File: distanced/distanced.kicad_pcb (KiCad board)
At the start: 2 copper layers, 25 parts, among them Y1 Crystal

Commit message: better schematic
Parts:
- added C11: 10uF, Capacitors_SMD:C_0402, F.Cu at (155.4, 114.0)
- added C12: 10uF, Capacitors_SMD:C_0402, F.Cu at (196.3, 130.7)
- added D1: LED, LEDs:LED_0402, F.Cu at (179.4, 145.6)
- added D2: LED_GREEN, LEDs:LED_0402, F.Cu at (128.8, 114.6)
- added D3: D_Small, Diodes_SMD:D_0603, F.Cu at (160.1, 134.7)
- added E1: Econn, Pin_Headers:Pin_Header_Angled_2x02_Pitch2.54mm, F.Cu at (200.9, 70.3)
- added J1: FTDI prog, Pin_Headers:Pin_Header_Angled_1x06_Pitch2.54mm, F.Cu at (169.0, 67.7)
- added J2: ICSP, Pin_Headers:Pin_Header_Straight_2x03_Pitch2.54mm, F.Cu at (194.6, 99.6)
- added N1: Nconn, Pin_Headers:Pin_Header_Angled_2x02_Pitch2.54mm, F.Cu at (201.1, 82.1)
- added Q1: BSS138, TO_SOT_Packages_SMD:SOT-23, F.Cu at (176.7, 118.5)
- added Q2: BSS138, TO_SOT_Packages_SMD:SOT-23, F.Cu at (175.1, 106.3)
- added R10: 10K, Resistors_SMD:R_0402, F.Cu at (132.6, 78.0)
- added R11: 10K, Resistors_SMD:R_0402, F.Cu at (115.8, 50.8)
- added R8: 10K, Resistors_SMD:R_0402, F.Cu at (142.5, 64.5)
- added R9: 10K, Resistors_SMD:R_0402, F.Cu at (108.2, 140.6)
- added S1: Sconn, Pin_Headers:Pin_Header_Angled_2x02_Pitch2.54mm, F.Cu at (201.5, 60.4)
- added U1: MIC5205-2.8, TO_SOT_Packages_SMD:SOT-23-5, F.Cu at (163.5, 119.7)
- added W1: Wconn, Pin_Headers:Pin_Header_Angled_2x02_Pitch2.54mm, F.Cu at (201.5, 52.0)
- C1, C3: value (none) -> 10uF
- C4: value (none) -> 0.1uF
- R1: value (none) -> 10K
- R4: value (none) -> 330
- SWRST1: footprint Buttons_Switches_THT:SW_PUSH_6mm_h4.3mm -> Buttons_Switches_SMD:SW_SPST_B3S-1000
- Y1: value Crystal -> Crystal_GND24; footprint Crystals:Crystal_SMD_2016-4pin_2.0x1.6mm -> Crystals:Crystal_SMD_3225-4pin_3.2x2.5mm_HandSoldering
- moved LSR1 103.6 mm to (166.7, 32.5)
- moved C8 67.0 mm to (79.3, 92.6)
- moved C7 59.7 mm to (78.9, 95.9)
- moved SWRST1 25.0 mm to (84.4, 81.8)
- moved Y1 3.05 mm to (86.6, 95.5), turned to 51 degrees
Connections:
- C10 pad 1: VCC -> +2V8
- C3 pad 1: VCC -> +3V3
- C4 pad 1: VCC -> +3V3
- C5 pad 1: VCC -> +3V3
- C9 pad 1: VCC -> +2V8
- LSR1 pad 1: VCC -> +2V8
- LSR1 pad 10: A5 -> 2.8_SCL
- LSR1 pad 11: VCC -> +2V8
- LSR1 pad 5: D3 -> Net-(D3-Pad2)
- LSR1 pad 9: A4 -> 2.8_SDA
- R2 pad 1: VCC -> +3V3
- R3 pad 1: VCC -> +3V3
- R5 pad 1: VCC -> +3V3
- R6 pad 1: VCC -> +2V8
- R7 pad 1: VCC -> +2V8
- R7 pad 2: D3 -> Net-(D3-Pad2)
- RS485 pad 8: VCC -> +3V3
- Vreg1 pad 5: VCC -> +3V3
- Y1 pad 2: Net-(C8-Pad1) -> GNDREF
- Y1 pad 3: (no net) -> Net-(C8-Pad1)
- Y1 pad 4: (no net) -> GNDREF
- uC1 pad 18: VCC -> +3V3
- uC1 pad 4: VCC -> +3V3
- uC1 pad 6: VCC -> +3V3

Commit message: first routing done, ready for revision and being lectured
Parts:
- removed C10: 4.7uF, Capacitors_SMD:C_0402
- removed C9: 100nF, Capacitors_SMD:C_0402
- removed D13, PWR: , LEDs:LED_0402
- removed D3: D_Small, Diodes_SMD:D_0603
- removed LSR1: VL53L0X, VL53L0X:VL53L0X
- removed N1: Nconn, Pin_Headers:Pin_Header_Angled_2x02_Pitch2.54mm
- removed R6, R7: 10K, Resistors_SMD:R_0402
- removed S1: Sconn, Pin_Headers:Pin_Header_Angled_2x02_Pitch2.54mm
- added C13: 100nF, Capacitors_SMD:C_0402, F.Cu at (148.1, 85.6)
- added C14: 4.7uF, Capacitors_SMD:C_0402, F.Cu at (148.1, 84.5)
- added D4: D_Small, Diodes_SMD:D_0603, F.Cu at (153.0, 80.7)
- added LSR2: VL53L0X, VL53L0X:VL53L0X, F.Cu at (148.1, 88.9)
- added R12: 10K, Resistors_SMD:R_0402, F.Cu at (147.2, 92.3)
- added R13: 10K, Resistors_SMD:R_0402, F.Cu at (149.0, 92.3)
- added REF**: MountingHole_3.2mm_M3_Pad, Mounting_Holes:MountingHole_3.2mm_M3_Pad, F.Cu at (148.0, 99.0)
- added REF**: MountingHole_3.2mm_M3_Pad, Mounting_Holes:MountingHole_3.2mm_M3_Pad, F.Cu at (148.0, 70.0)
- C1, C11, C12, C3, C4, C7, C8, E1, J1, Q1, Q2, R10, R11, R2, R3, R8, R9, RS485, U1, Vreg1, W1, Y1, uC1: moved to B.Cu
- J2: footprint Pin_Headers:Pin_Header_Straight_2x03_Pitch2.54mm -> Pin_Headers:Pin_Header_Angled_2x03_Pitch2.54mm; moved to B.Cu
- moved R9 69.3 mm to (157.5, 91.8), turned to 180 degrees
- moved C7 68.6 mm to (144.1, 74.5)
- moved W1 67.1 mm to (138.5, 75.0), turned to 180 degrees
- moved C8 66.0 mm to (144.2, 80.4), turned to 180 degrees
- moved E1 65.8 mm to (138.5, 91.0), turned to 180 degrees
- moved C12 64.7 mm to (146.9, 88.9), turned to 90 degrees
- moved SWRST1 63.5 mm to (147.9, 78.7), turned to 90 degrees
- moved D1 63.4 mm to (152.0, 88.4), turned to 270 degrees
- moved Y1 60.4 mm to (144.3, 77.5), turned to 0 degrees
- moved J2 59.0 mm to (138.5, 81.5), turned to 180 degrees
- moved uC1 58.7 mm to (153.8, 79.1)
- moved C6 56.2 mm to (143.0, 74.7), turned to 180 degrees
- moved R11 54.5 mm to (156.9, 86.6), turned to 270 degrees
- moved C5 49.2 mm to (152.8, 78.1), turned to 90 degrees
- moved RS485 47.6 mm to (144.2, 84.0), turned to 0 degrees
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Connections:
- C11 pad 1: Net-(C11-Pad1) -> +3V3
- C3 pad 2: Net-(C3-Pad2) -> GNDREF
- C4 pad 2: Net-(C3-Pad2) -> GNDREF
- R1 pad 2: Net-(C3-Pad2) -> GNDREF
- Vreg1 pad 3: Net-(Vreg1-Pad3) -> RAW
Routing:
- net GNDREF: track 0.00 -> 151.1 mm, vias 0 -> 8
- net +3V3: track 0.00 -> 116.5 mm, vias 0 -> 9
- net RAW: track 0.00 -> 93.3 mm
- net DRT: track 0.00 -> 82.7 mm
- net D13: track 0.00 -> 53.6 mm, vias 0 -> 1
- net D11: track 0.00 -> 46.2 mm, vias 0 -> 2
- net B: track 0.00 -> 39.2 mm, vias 0 -> 4
- net A: track 0.00 -> 32.8 mm, vias 0 -> 1
- net D4: track 0.00 -> 31.1 mm, vias 0 -> 5
- net RXI: track 0.00 -> 31.1 mm, vias 0 -> 2
- net +2V8: track 0.00 -> 30.0 mm, vias 0 -> 4
- net D12: track 0.00 -> 26.3 mm
- net TXO: track 0.00 -> 26.3 mm, vias 0 -> 3
- net A4: track 0.00 -> 21.2 mm
- net Net-(D4-Pad2): track 0.00 -> 20.8 mm, vias 0 -> 6
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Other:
- board outline added: 29 x 41 mm
- net class Default: clearance 0.2 -> 0.00889
- rule trace_clearance: 0.2 -> 0.00889
- rule trace_min: 0.2 -> 0.0889

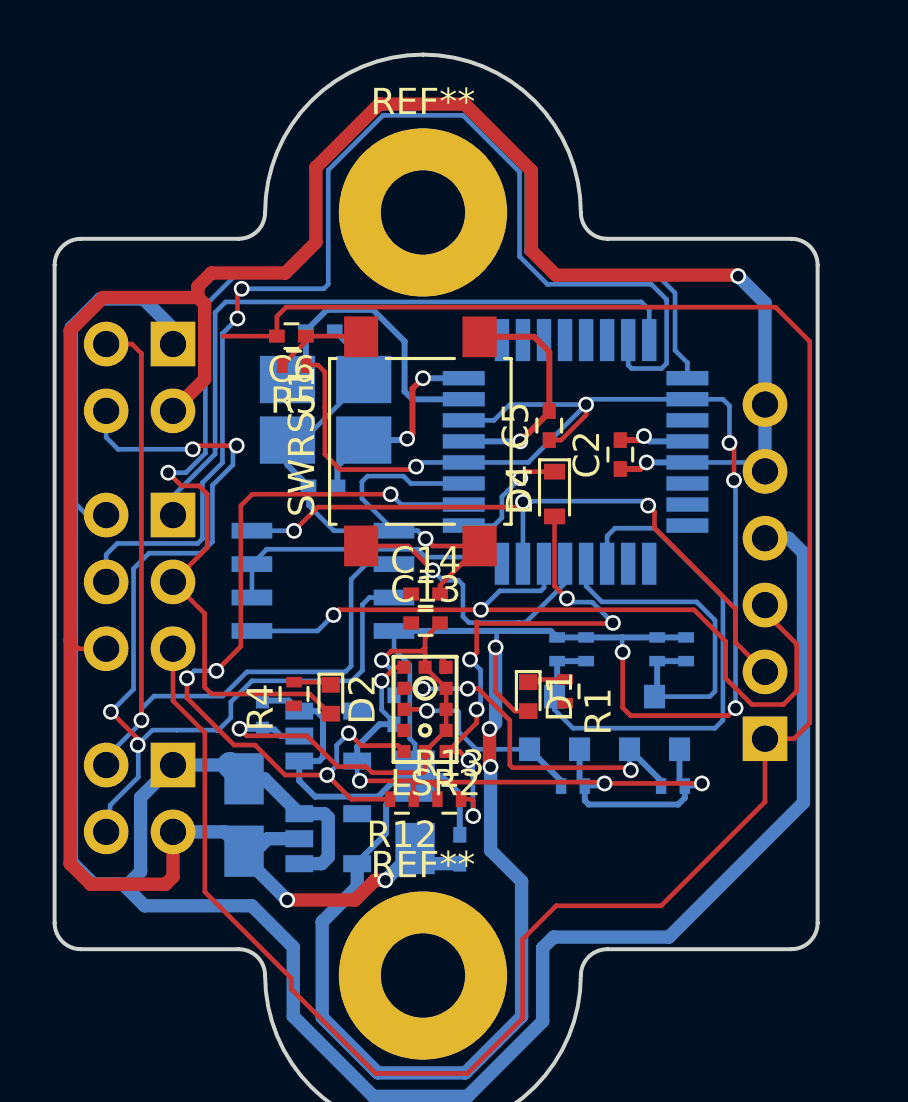
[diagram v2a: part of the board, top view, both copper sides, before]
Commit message: modified reference text on the board
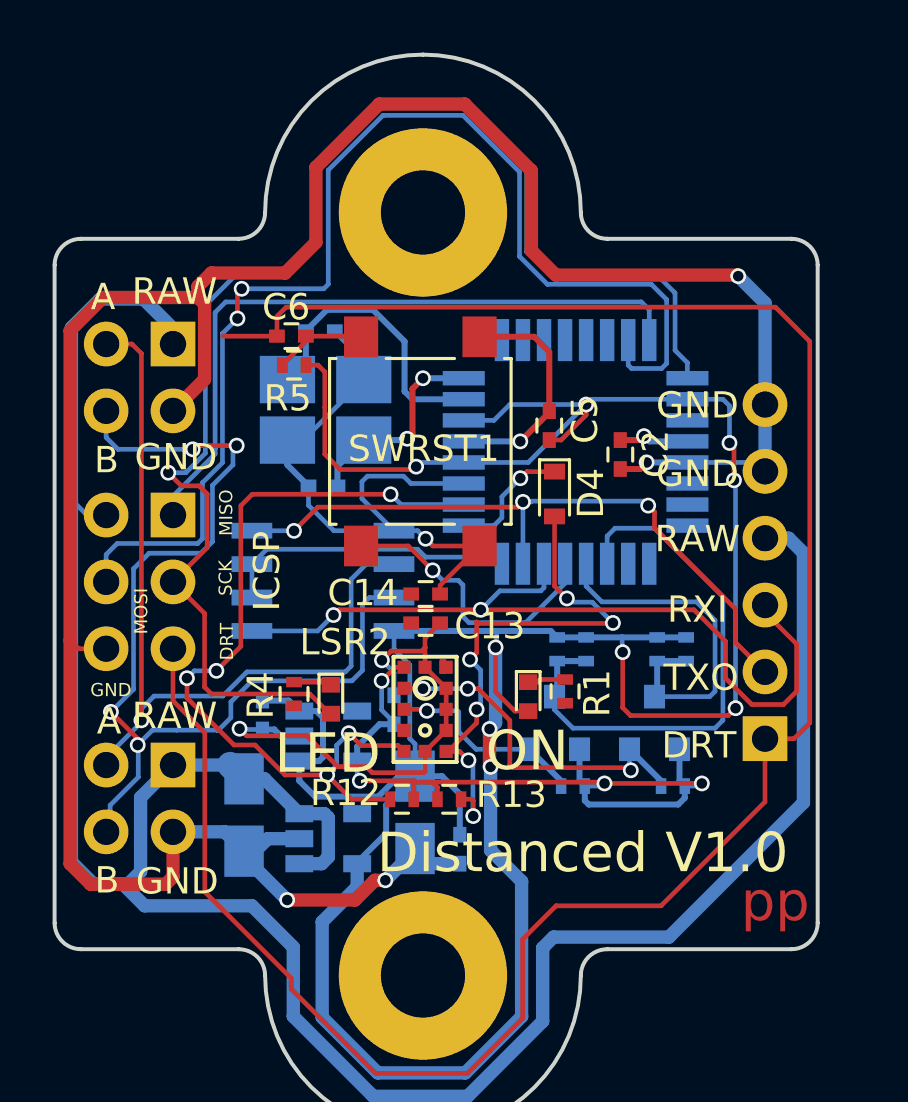
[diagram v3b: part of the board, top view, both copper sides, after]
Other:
- board text added: "A"
- board text added: "B"
- board text added: "DRT"
- board text added: "Distanced V1.0"
- board text added: "GND"
- board text added: "ICSP"
- board text added: "LED"
- board text added: "MISO"
- board text added: "MOSI"
- board text added: "ON"
- board text added: "RAW"
- board text added: "RXI"
- board text added: "SCK"
- board text added: "TXO"
- board text added: "pp"

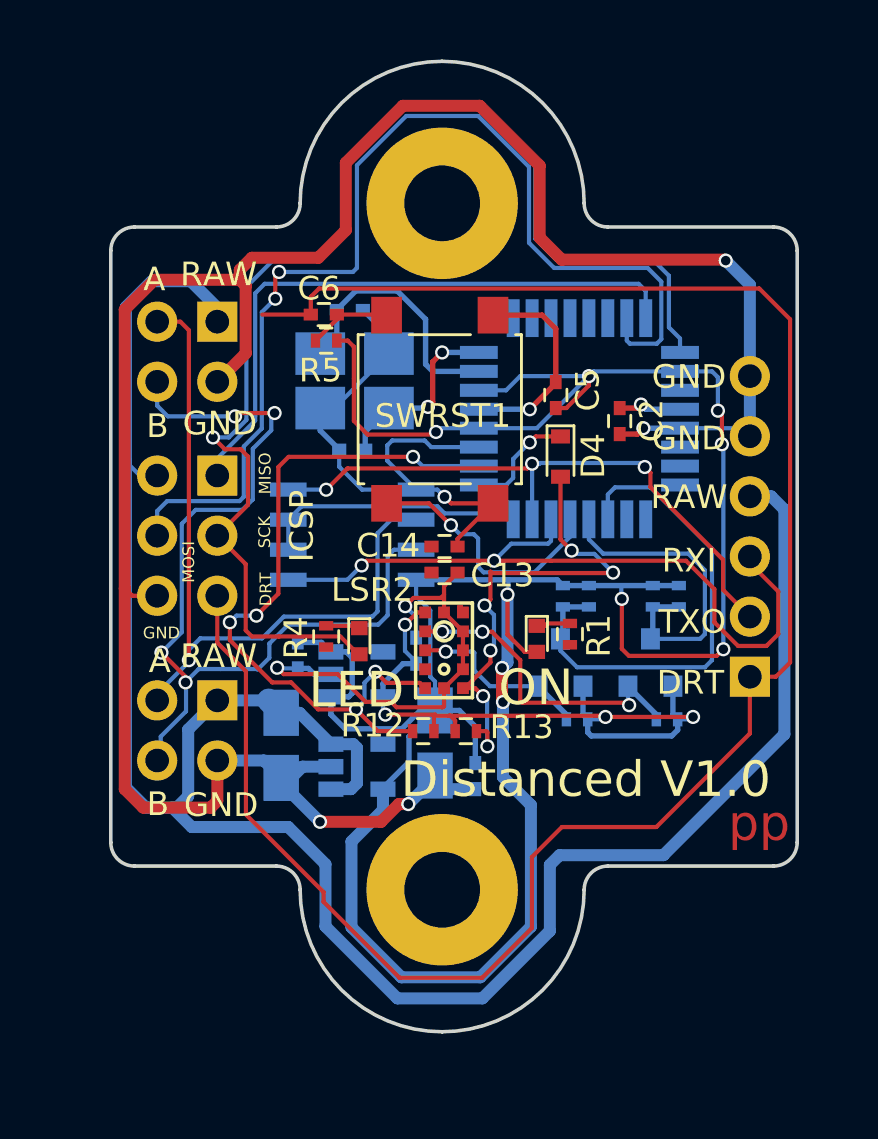
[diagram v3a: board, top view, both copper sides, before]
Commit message: Updating the PCB to fit the requirements for PCBway
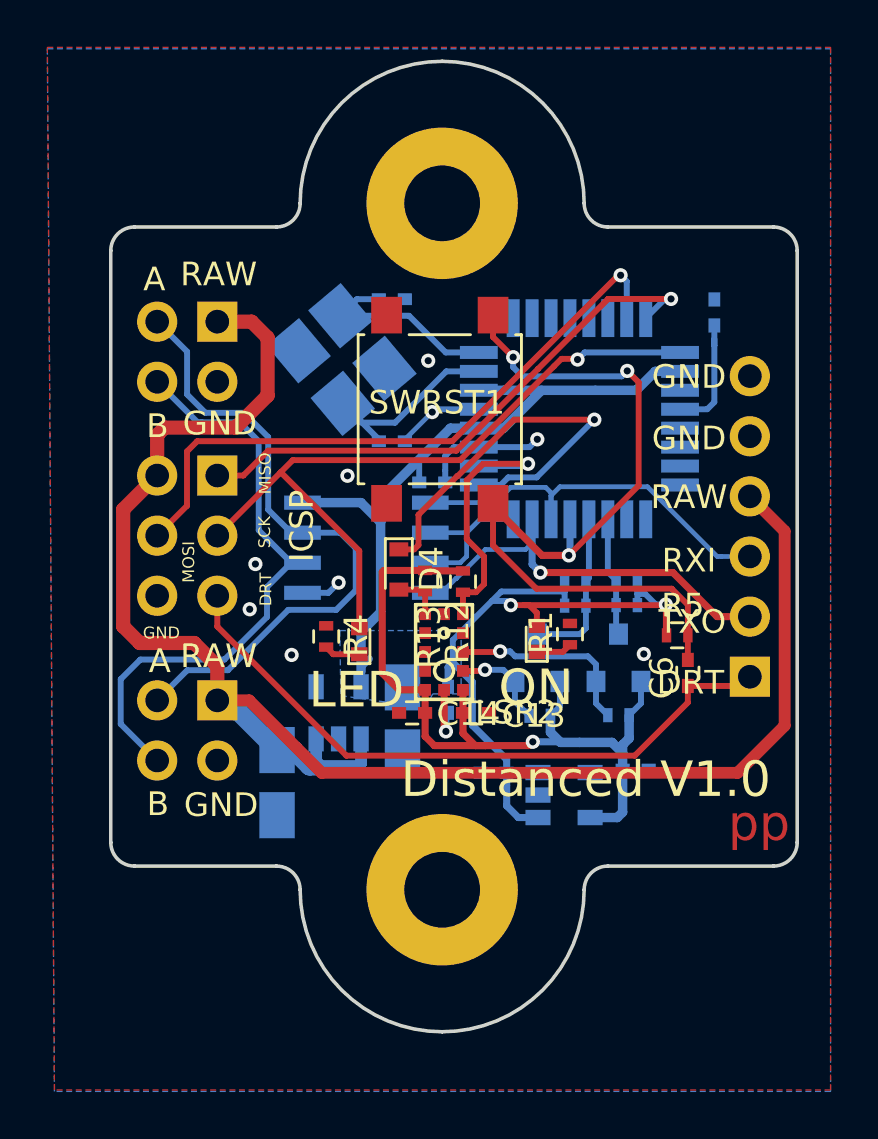
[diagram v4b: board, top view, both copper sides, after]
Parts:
- C2, C5: moved to B.Cu
- moved C6 21.6 mm to (158.4, 89.8), turned to 270 degrees
- moved R5 19.4 mm to (157.9, 88.2), turned to 0 degrees
- moved C12 10.5 mm to (156.2, 93.9), turned to 0 degrees
- moved U1 10.1 mm to (153.2, 95.0)
- moved C11 9.64 mm to (150.2, 94.0), turned to 180 degrees
- moved D4 8.33 mm to (146.2, 85.5)
- moved C14 7.16 mm to (146.7, 91.5), turned to 180 degrees
- moved R13 6.57 mm to (147.3, 86.0), turned to 270 degrees
- moved C8 6.57 mm to (145.9, 74.0), turned to 0 degrees
- moved R12 6.54 mm to (148.9, 86.0), turned to 270 degrees
- moved C5 6.39 mm to (147.6, 81.8), turned to 0 degrees
- moved C2 6.09 mm to (159.5, 74.6), turned to 270 degrees
- moved C13 6.08 mm to (149.4, 91.5)
- moved C7 5.83 mm to (145.9, 80.0)
- moved R9 5.38 mm to (152.1, 91.7)
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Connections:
- E1 pad 2: A -> B
- E1 pad 4: B -> A
- LSR2 pad 8: Net-(LSR2-Pad8) -> (no net)
- U1 pad 4: Net-(U1-Pad4) -> (no net)
- Vreg1 pad 4: Net-(Vreg1-Pad4) -> (no net)
- W1 pad 2: A -> B
- W1 pad 4: B -> A
- uC1 pad 10: D6 -> (no net)
- uC1 pad 11: D7 -> (no net)
- uC1 pad 12: D8 -> (no net)
- uC1 pad 13: D9 -> (no net)
- uC1 pad 14: D10 -> (no net)
- uC1 pad 19: A6 -> (no net)
- uC1 pad 22: A7 -> (no net)
- uC1 pad 23: A0 -> (no net)
- uC1 pad 24: A1 -> (no net)
- uC1 pad 25: A2 -> (no net)
- uC1 pad 26: A3 -> (no net)
- uC1 pad 9: D5 -> (no net)
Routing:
- net GNDREF: track 151.1 -> 13.3 mm, vias 8 -> 10
- net DRT: track 82.7 -> 27.9 mm
- net +3V3: track 116.5 -> 67.4 mm, vias 9 -> 2
- net D13: track 53.6 -> 30.8 mm
- net RAW: track 93.3 -> 70.8 mm
- net Net-(C6-Pad1): track 14.6 -> 35.9 mm, vias 1 -> 3
- net D4: track 31.1 -> 11.6 mm, vias 5 -> 1
- net D11: track 46.2 -> 27.4 mm, vias 2 -> 1
- net Net-(D4-Pad2): track 20.8 -> 2.09 mm, vias 6 -> 0
- net A4: track 21.2 -> 5.04 mm
- net RXI: track 31.1 -> 17.4 mm, vias 2 -> 0
- net D3: track 4.77 -> 17.3 mm
- net B: track 39.2 -> 27.3 mm, vias 4 -> 0
- net 2.8_SCL: track 13.6 -> 4.12 mm, vias 3 -> 1
- net TXO: track 26.3 -> 18.2 mm, vias 3 -> 1
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- added copper zone on B.Cu, net +3V3
- added copper zone on B.Cu, net GNDREF
- added copper zone on F.Cu, net GNDREF
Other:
- net class Default: clearance 0.00889 -> 0.15; via_drill 0.4 -> 0.3
- rule trace_clearance: 0.00889 -> 0.15
- rule trace_min: 0.0889 -> 0.15
- rule via_min_size: 0.4 -> 0.5

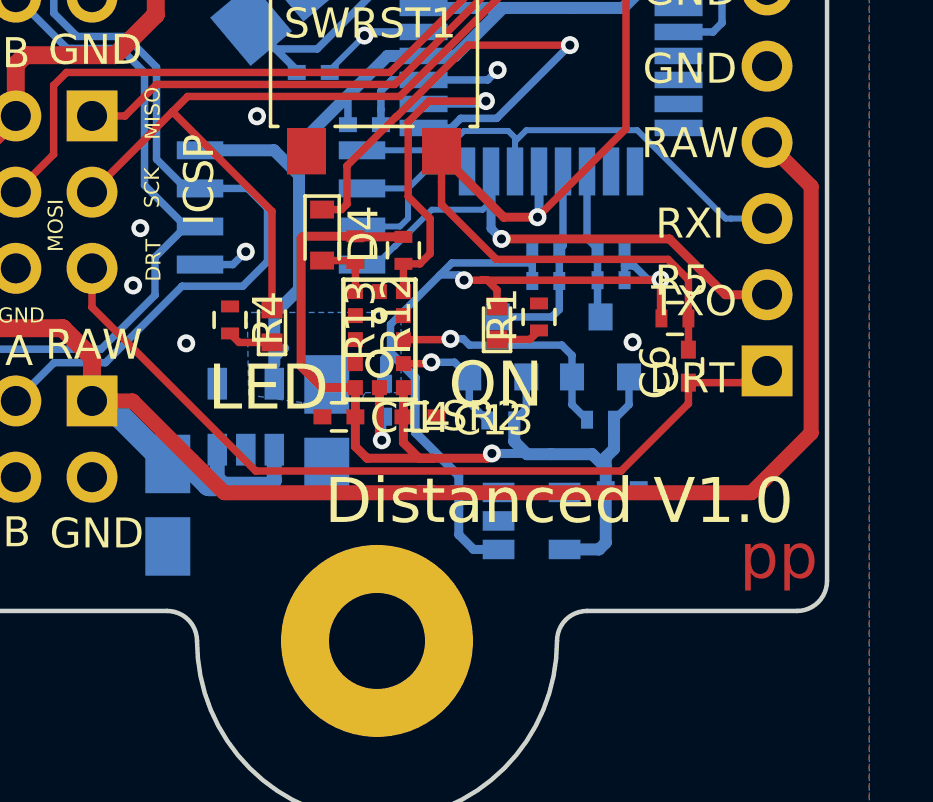
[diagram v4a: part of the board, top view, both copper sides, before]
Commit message: Ready for production
Modified silk screen to easy soldering and debugging
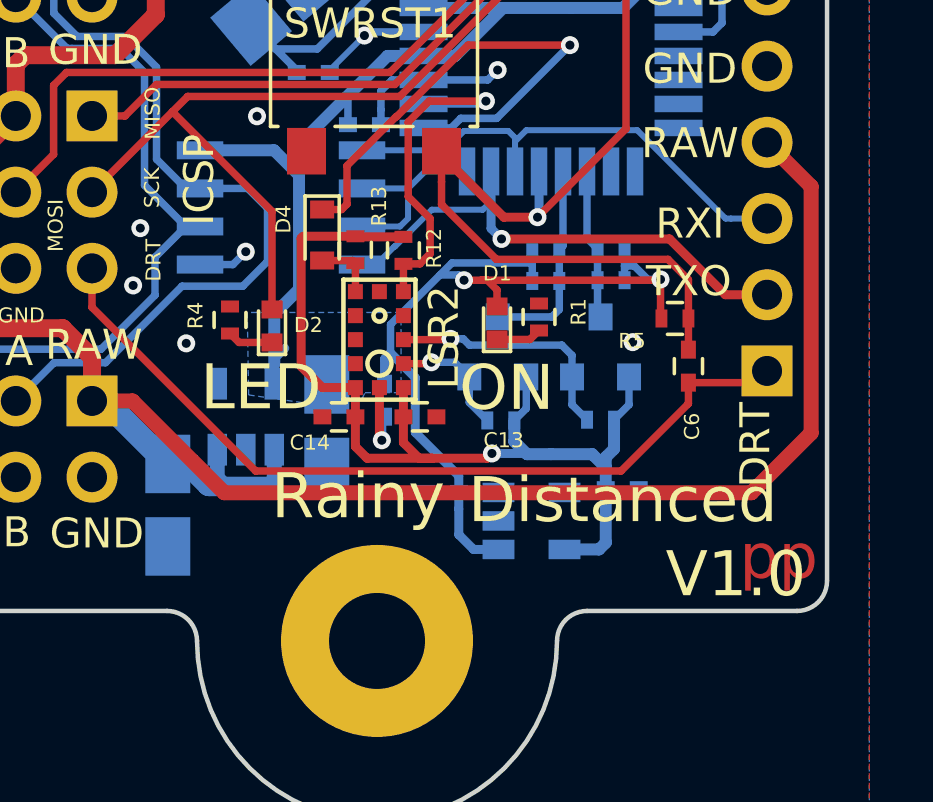
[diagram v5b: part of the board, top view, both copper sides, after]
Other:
- board text added: "Distanced"
- board text added: "El Bart"
- board text added: "El Pepe"
- board text added: "Rainy"
- board text added: "V1.0"
- board text removed: "Distanced V1.0"
